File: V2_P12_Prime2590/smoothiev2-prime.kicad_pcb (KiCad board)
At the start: 4 copper layers, 110 x 110 mm, 453 parts, among them J1 USB_B, J10 Conn_01x02, J11 Conn_01x02, J12 Conn_01x02, J13 Conn_01x02, J14 Conn_01x02, J15 Conn_01x02, J16 Conn_01x02, J17 Conn_01x02, J18 Conn_01x02, J19 Conn_01x02, J2 USB_A, J20 Conn_01x02, J21 Conn_01x02, J22 Conn_01x02, J23 Conn_01x02, J24 Conn_01x03, J25 Conn_01x03, J26 Conn_01x03, J27 Conn_01x03, J28 Conn_01x03, J29 Conn_01x03, J3 Micro_SD_Card_Det, J30 Conn_01x03_Male, J31 Conn_01x04, J32 Conn_02x05_Odd_Even, J33 Conn_02x05_Odd_Even, J34 Conn_02x05_Odd_Even, J35 Conn_02x05_Odd_Even, J36 Conn_02x05_Odd_Even, J37 Conn_02x05_Odd_Even, J38 Conn_02x05_Odd_Even, J39 Conn_02x05_Odd_Even, J4 RJ45_Hanrun_HR911105A, J40 Conn_02x05_Odd_Even, J41 Conn_ARM_JTAG_SWD_10, J42 Conn_01x02, J43 Conn_01x02, J44 Conn_01x02, J45 Conn_01x02, J5 Screw_Terminal_01x04, J6 Screw_Terminal_01x04, J7 Screw_Terminal_01x04, J8 Screw_Terminal_01x04, J9 Conn_01x02, Q1 Si4542DY, Q10 Si4542DY, Q11 Si4542DY, Q12 Si4542DY, Q13 Si4542DY, Q14 Si4542DY, Q15 Si4542DY, Q16 Si4542DY, Q17 WSD3066DN33, Q18 WSD3066DN33, Q19 WSD3066DN33, Q2 Si4542DY, Q20 WSD3066DN33, Q21 WSD3066DN33, Q22 WSD3066DN33, Q23 CJ2301 S1, Q24 CJ2301 S1, Q25 WSD30L40DN, Q26 2N7002, Q27 MBT3906DW1, Q28 SQ3493EV, Q29 MBT3906DW1, Q3 Si4542DY, Q30 SQ3493EV, Q31 MBT3906DW1, Q32 SQ3493EV, Q4 Si4542DY, Q5 Si4542DY, Q6 Si4542DY, Q7 Si4542DY, Q8 Si4542DY, Q9 Si4542DY, SW1 SW_Push, SW2 TS-1185EC-C-D-B, U1 LAN8720A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

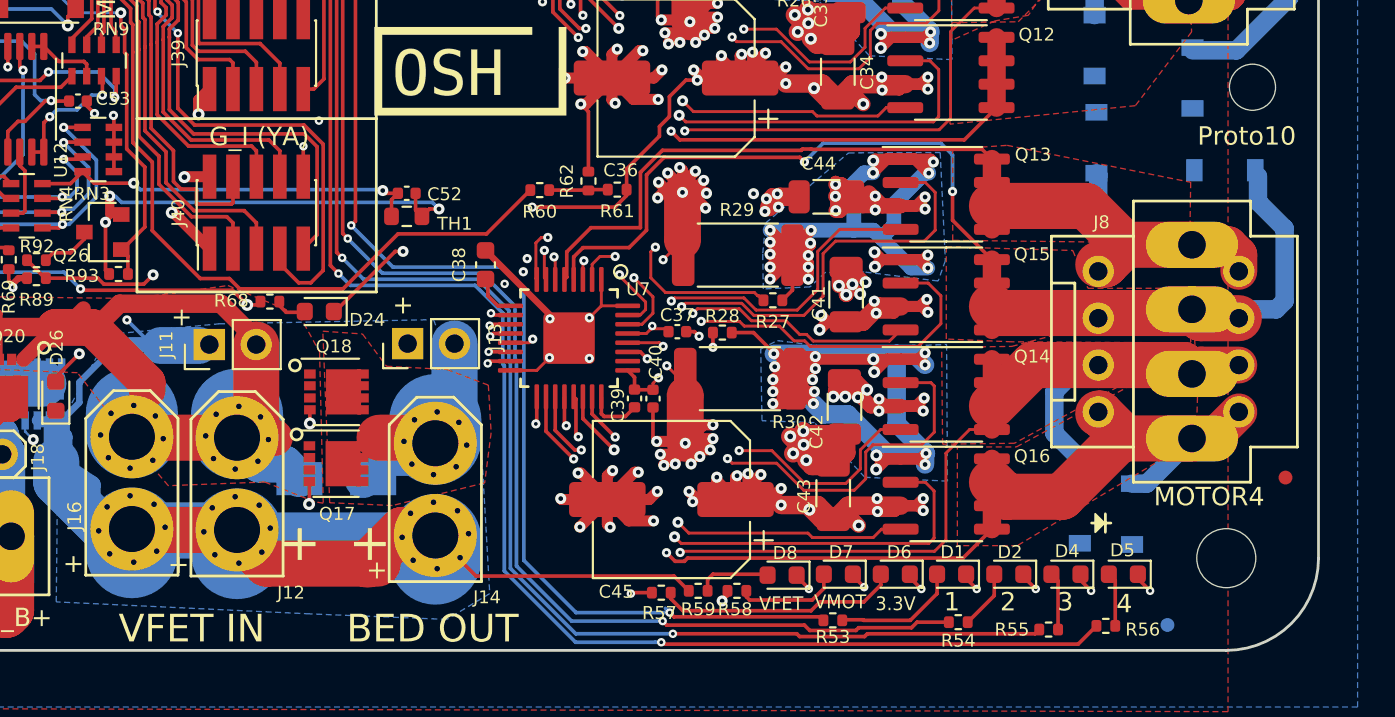
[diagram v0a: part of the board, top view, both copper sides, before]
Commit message: Added 3d models, renders and stepfiles
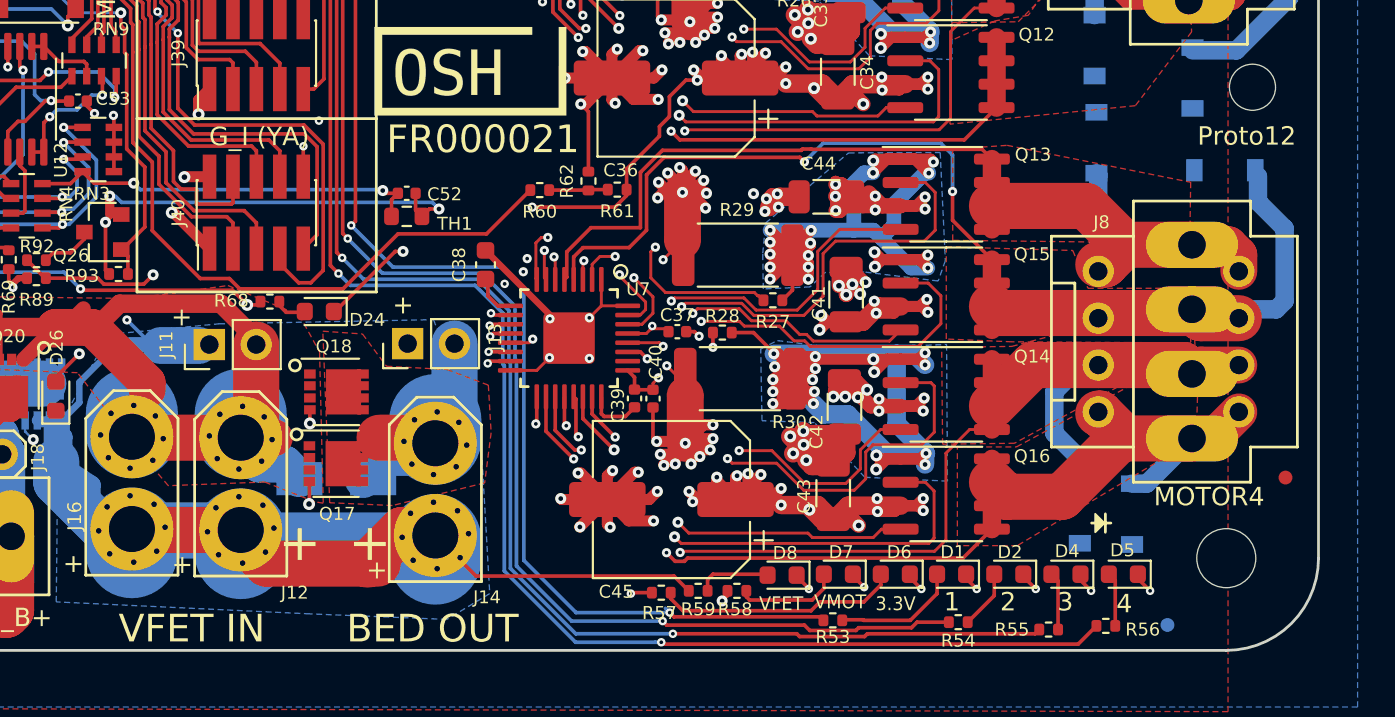
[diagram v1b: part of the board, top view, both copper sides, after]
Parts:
- moved LOGO1 9.64 mm to (145.5, 88.5)
- moved LOGO3 1.36 mm to (162.7, 51.4)
- moved J12 0.20 mm to (151.4, 139.0)
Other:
- board text added: "6x Endstop connectors supporting Min and Max stops for X, Y, and Z"
- board text added: "9 GADGETEER Gadgeteer standard connectors give a total of 63 GPIO capable pins"
- board text added: "Comparator buffered probe input allows Trigger voltages from 3-45v (Ranges switched by jumpers)"
- board text added: "Controlled MOSFETs 4x High side controlled mosfets 2 for fan 2 for hotends"
- board text added: "Developed in multiple open source communities based on the feedback from our users and developers. Thanks to all who give back to open source. Extra special thanks to: Kliment and Wolfmanjm"
- board text added: "FR000021"
- board text added: "High Current MOSFET Out Dual mosfet for heated bed"
- board text added: "MOSFET POWER 2x XT30 connector for 12V - 24V input"
- board text added: "Proto12"
- board text added: "STEPPER MOTORS 4x TMC2590 bipolar stepper drivers configured for 24V and 4.3A maximums"
- board text added: "https://github.com/Smoothieware/SmoothieV2/wiki"
- board text removed: "7x Endstop connectors supporting Min and Max stops for X, Y, and Z plus a Probe"
- board text removed: "GADGET as many gadget connectors as possible with spare GPIO"
- board text removed: "LARGE MOSFET large mosfet for heated bed"
- board text removed: "MOSFET POWER XT30 connector for 12V - 24V input"
- board text removed: "PARALLEL FLASH 64Mbit (8MByte) of high speed flash"
- board text removed: "Proto10"
- board text removed: "SMALL MOSFET 3x small mosfets one for fan two for hotends"
- board text removed: "STEPPER MOTORS 4x TMC2660 bipolar stepper drivers configured for 24V and 2.8A maximums"
